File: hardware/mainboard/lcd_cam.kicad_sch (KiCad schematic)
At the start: 59 parts

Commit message: ERC fixes
Signed-off-by: gatecat <gatecat@ds0.me>
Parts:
- gave numbers to parts that had none: 59
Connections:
- net DSI0A_D0-: no longer LCD2.11 (DSI_D0-_A)
- net FRONT_LCD_TE renamed RIGHT_LCD_TE
- new net DSI1A_D0-: LCD2.11 (DSI_D0-_A)

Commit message: Add some footprint mappings
Signed-off-by: gatecat <gatecat@ds0.me>
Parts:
- C65, C66, C69, C70: footprint (none) -> Capacitor_SMD:C_0402_1005Metric
- C67, C74, C75: footprint (none) -> Capacitor_SMD:C_1206_3216Metric
- C68, C71, C72, C73, C76: footprint (none) -> Capacitor_SMD:C_0603_1608Metric
- CAM1, CAM2: footprint (none) -> meowality:54548-2271
- D20, D21, D22: footprint (none) -> Diode_SMD:D_SMA
- L6, L8: footprint (none) -> Inductor_SMD:L_Taiyo-Yuden_NR-50xx
- LCD1, LCD2: footprint (none) -> meowality:245863060104829
- R63, R64, R65, R66, R67, R68, R69, R70, R71, R72, R73, R74, R75, R76, R77, R78, R79, R80, R81, R82, R83, R84, R85, R86, R87, R88, R89, R90, R91, R92, R93, R94: footprint (none) -> Resistor_SMD:R_0402_1005Metric

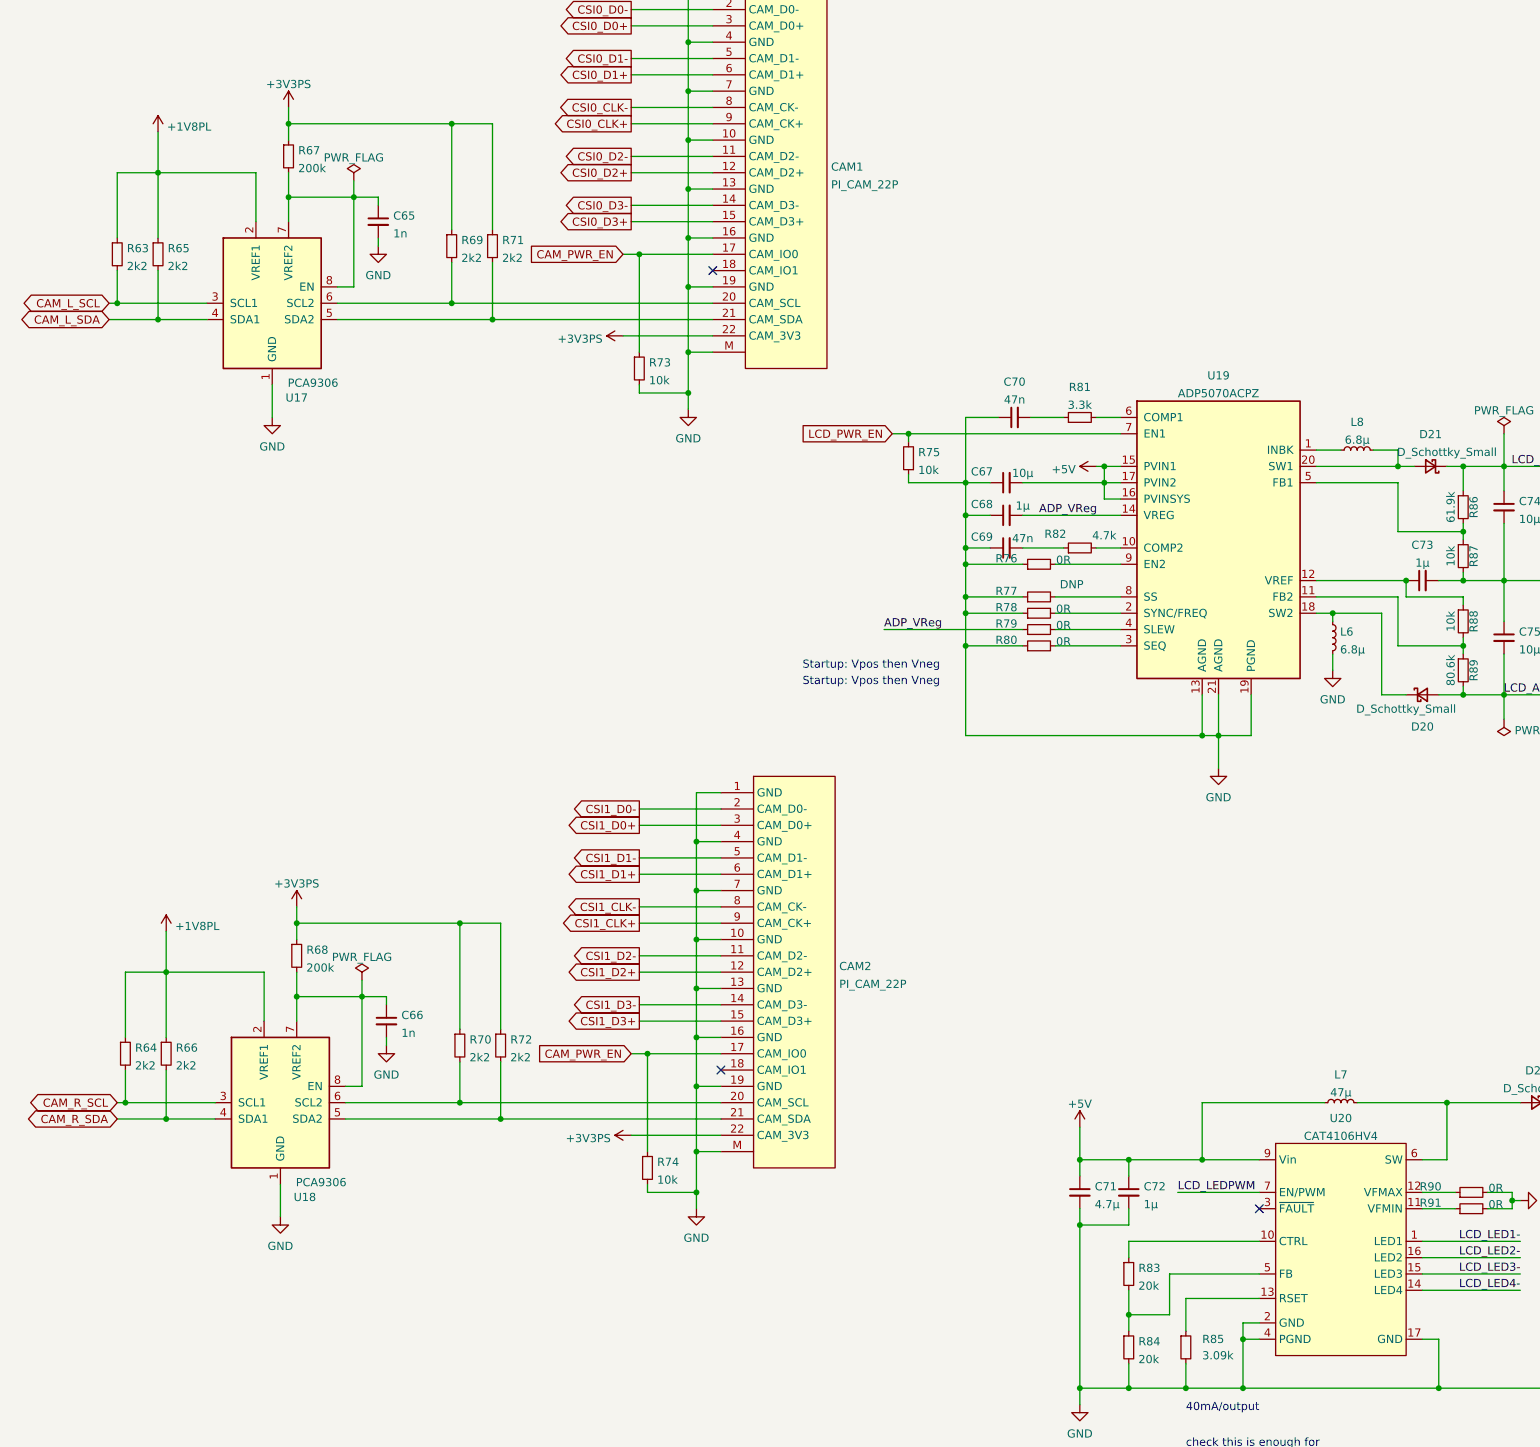
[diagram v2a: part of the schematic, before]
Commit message: Footprint assignments and related fixes
Signed-off-by: gatecat <gatecat@ds0.me>
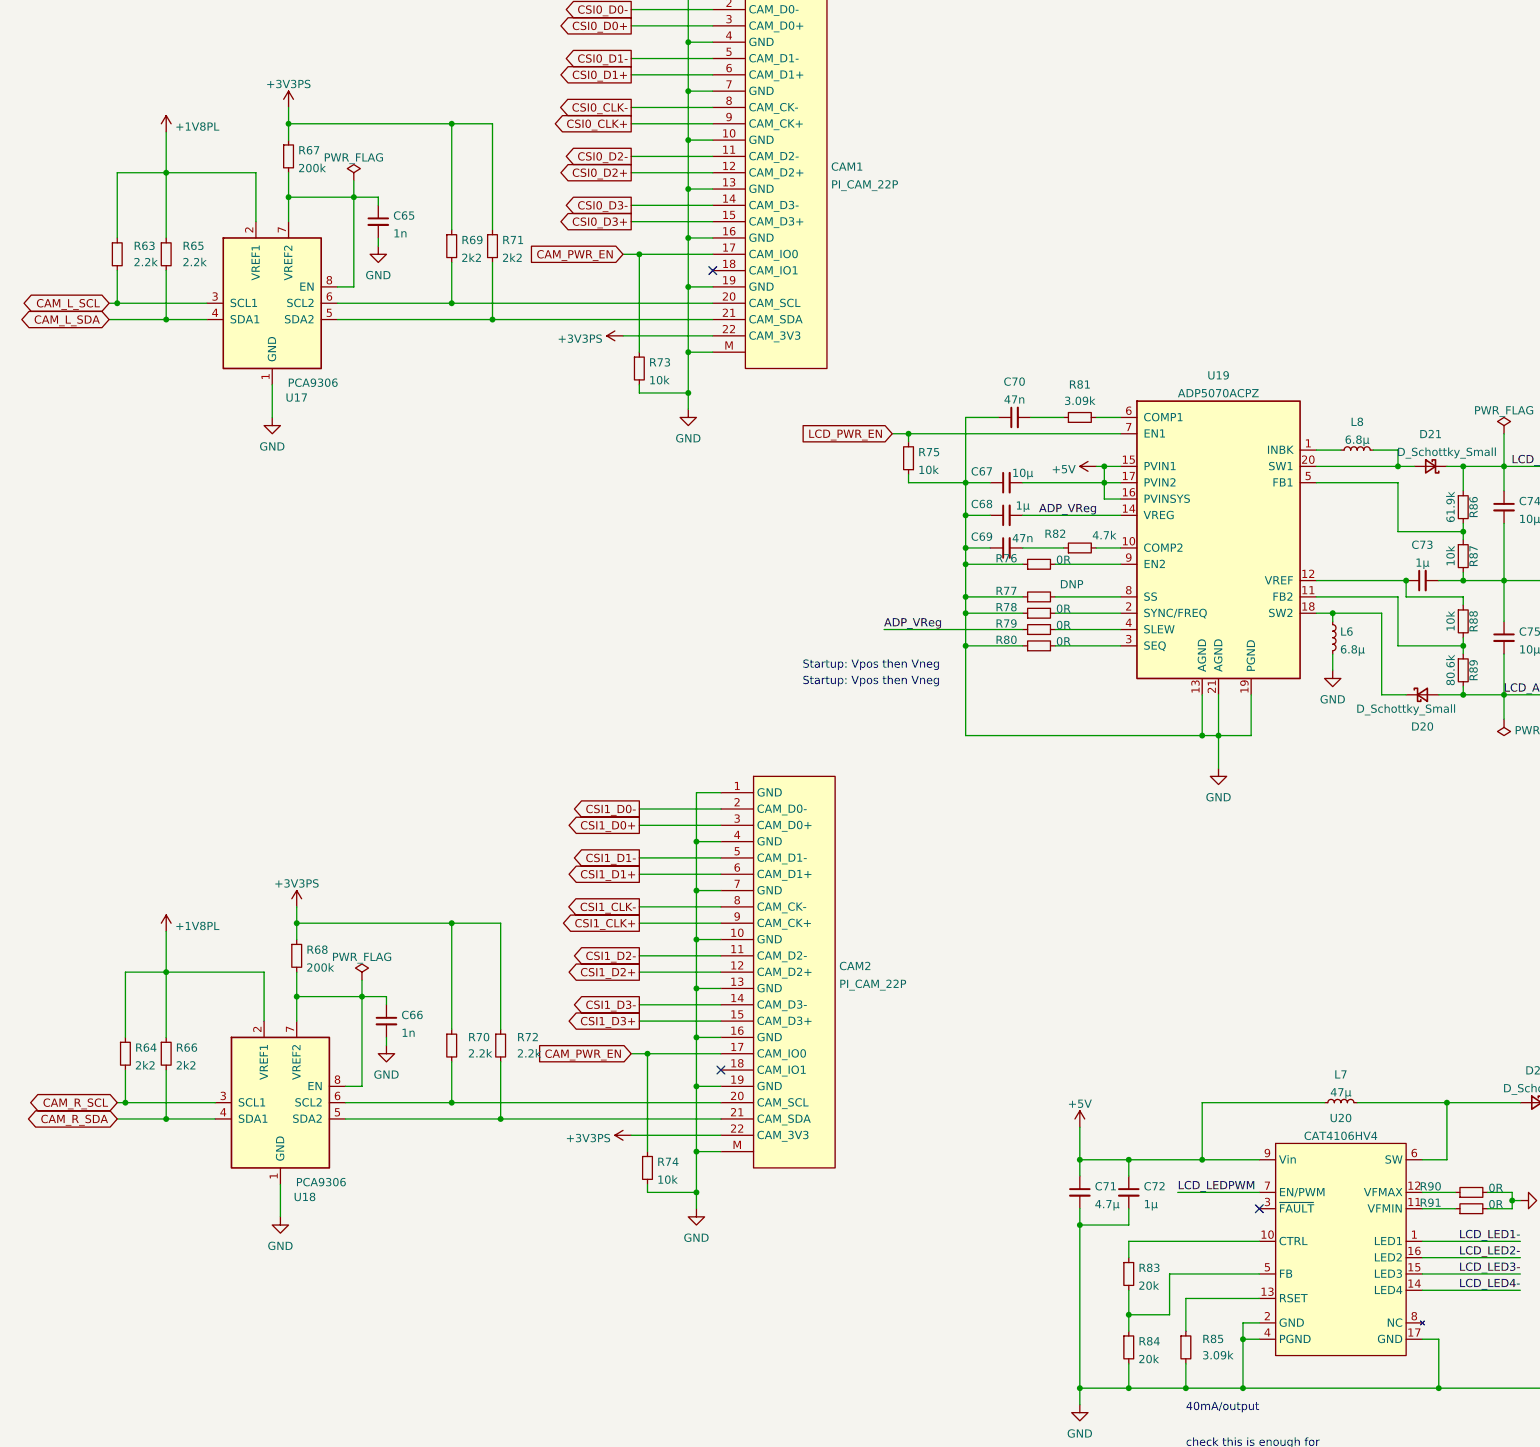
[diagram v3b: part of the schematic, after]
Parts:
- R63, R65, R70, R72: value 2k2 -> 2.2k
- R81: value 3.3k -> 3.09k
- TP1: footprint (none) -> TestPoint:TestPoint_Pad_D2.0mm
- U17, U18: footprint (none) -> Package_SO:TSSOP-8_3x3mm_P0.65mm
- U19: footprint (none) -> Package_DFN_QFN:QFN-20-1EP_4x4mm_P0.5mm_EP2.6x2.6mm
- U20: footprint (none) -> Package_DFN_QFN:QFN-16-1EP_4x4mm_P0.65mm_EP2.1x2.1mm
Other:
- moved on the sheet: R65, R70
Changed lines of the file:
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@@
   (junction (at 201.93 234.95) (diameter 0) (color 0 0 0 0)
   )
-  (junction (at 97.79 201.93) (diameter 0) (color 0 0 0 0)
+  (junction (at 96.52 201.93) (diameter 0) (color 0 0 0 0)
   )
   (junction (at 176.53 118.11) (diameter 0) (color 0 0 0 0)
@@
   (junction (at 72.39 185.42) (diameter 0) (color 0 0 0 0)
   )
-  (junction (at 97.79 173.99) (diameter 0) (color 0 0 0 0)
+  (junction (at 96.52 173.99) (diameter 0) (color 0 0 0 0)
   )
   (junction (at 201.93 246.38) (diameter 0) (color 0 0 0 0)
@@
   (junction (at 52.07 181.61) (diameter 0) (color 0 0 0 0)
   )
-  (junction (at 50.8 57.15) (diameter 0) (color 0 0 0 0)
+  (junction (at 52.07 57.15) (diameter 0) (color 0 0 0 0)
   )
   (junction (at 176.53 115.57) (diameter 0) (color 0 0 0 0)
@@
   (junction (at 356.87 31.75) (diameter 0) (color 0 0 0 0)
   )
-  (junction (at 50.8 80.01) (diameter 0) (color 0 0 0 0)
+  (junction (at 52.07 80.01) (diameter 0) (color 0 0 0 0)
   )
   (junction (at 254 138.43) (diameter 0) (color 0 0 0 0)
@@
     (stroke (width 0) (type default) (color 0 0 0 0))
   )
-  (wire (pts (xy 50.8 50.8) (xy 50.8 57.15))
+  (wire (pts (xy 52.07 50.8) (xy 52.07 57.15))
     (stroke (width 0) (type default) (color 0 0 0 0))
   )
@@
     (stroke (width 0) (type default) (color 0 0 0 0))
   )
-  (wire (pts (xy 50.8 57.15) (xy 66.04 57.15))
+  (wire (pts (xy 52.07 57.15) (xy 66.04 57.15))
     (stroke (width 0) (type default) (color 0 0 0 0))
   )
@@
     (stroke (width 0) (type default) (color 0 0 0 0))
   )
-  (wire (pts (xy 50.8 72.39) (xy 50.8 80.01))
+  (wire (pts (xy 52.07 72.39) (xy 52.07 80.01))
     (stroke (width 0) (type default) (color 0 0 0 0))
   )
@@
     (stroke (width 0) (type default) (color 0 0 0 0))
   )
-  (wire (pts (xy 44.45 57.15) (xy 50.8 57.15))
+  (wire (pts (xy 44.45 57.15) (xy 52.07 57.15))
     (stroke (width 0) (type default) (color 0 0 0 0))
   )
@@
     (stroke (width 0) (type default) (color 0 0 0 0))
   )
-  (wire (pts (xy 72.39 173.99) (xy 97.79 173.99))
+  (wire (pts (xy 72.39 173.99) (xy 96.52 173.99))
     (stroke (width 0) (type default) (color 0 0 0 0))
   )
@@
     (stroke (width 0) (type default) (color 0 0 0 0))
   )
-  (wire (pts (xy 97.79 195.58) (xy 97.79 201.93))
+  (wire (pts (xy 96.52 195.58) (xy 96.52 201.93))
     (stroke (width 0) (type default) (color 0 0 0 0))
   )
@@
     (stroke (width 0) (type default) (color 0 0 0 0))
   )
-  (wire (pts (xy 97.79 173.99) (xy 97.79 190.5))
+  (wire (pts (xy 96.52 173.99) (xy 96.52 190.5))
     (stroke (width 0) (type default) (color 0 0 0 0))
   )
@@
     (stroke (width 0) (type default) (color 0 0 0 0))
   )
-  (wire (pts (xy 97.79 201.93) (xy 138.43 201.93))
+  (wire (pts (xy 96.52 201.93) (xy 138.43 201.93))
     (stroke (width 0) (type default) (color 0 0 0 0))
   )
@@
     (stroke (width 0) (type default) (color 0 0 0 0))
   )
-  (wire (pts (xy 104.14 173.99) (xy 97.79 173.99))
+  (wire (pts (xy 104.14 173.99) (xy 96.52 173.99))
     (stroke (width 0) (type default) (color 0 0 0 0))
   )
@@
     (stroke (width 0) (type default) (color 0 0 0 0))
   )
-  (wire (pts (xy 43.18 80.01) (xy 50.8 80.01))
+  (wire (pts (xy 43.18 80.01) (xy 52.07 80.01))
     (stroke (width 0) (type default) (color 0 0 0 0))
   )
@@
     (stroke (width 0) (type default) (color 0 0 0 0))
   )
-  (wire (pts (xy 50.8 80.01) (xy 58.42 80.01))
+  (wire (pts (xy 52.07 80.01) (xy 58.42 80.01))
     (stroke (width 0) (type default) (color 0 0 0 0))
   )
@@
     (stroke (width 0) (type default) (color 0 0 0 0))
   )
-  (wire (pts (xy 80.01 201.93) (xy 97.79 201.93))
+  (wire (pts (xy 80.01 201.93) (xy 96.52 201.93))
     (stroke (width 0) (type default) (color 0 0 0 0))
   )
@@
     (stroke (width 0) (type default) (color 0 0 0 0))
   )
-  (wire (pts (xy 50.8 57.15) (xy 50.8 67.31))
+  (wire (pts (xy 52.07 57.15) (xy 52.07 67.31))
     (stroke (width 0) (type default) (color 0 0 0 0))
   )
@@
     (pin "2")
   )
-  (symbol (lib_id "meowality:+1V8PL") (at 50.8 50.8 0) (unit 1)
+  (symbol (lib_id "meowality:+1V8PL") (at 52.07 50.8 0) (unit 1)
     (in_bom yes) (on_board yes) (fields_autoplaced)
-    (property "Reference" "#PWR0354" (id 0) (at 50.8 54.61 0)
+    (property "Reference" "#PWR0354" (id 0) (at 52.07 54.61 0)
       (effects (font (size 1.27 1.27)) hide)
     )
-    (property "Value" "+1V8PL" (id 1) (at 52.197 50.009 0)
+    (property "Value" "+1V8PL" (id 1) (at 53.467 50.009 0)
       (effects (font (size 1.27 1.27)) (justify left))
     )
-    (property "Footprint" "" (id 2) (at 50.8 50.8 0)
+    (property "Footprint" "" (id 2) (at 52.07 50.8 0)
       (effects (font (size 1.27 1.27)) hide)
     )
-    (property "Datasheet" "" (id 3) (at 50.8 50.8 0)
+    (property "Datasheet" "" (id 3) (at 52.07 50.8 0)
       (effects (font (size 1.27 1.27)) hide)
     )
@@
       (effects (font (size 1.27 1.27)) (justify left))
     )
-    (property "Footprint" "" (id 2) (at 370.84 123.19 0)
+    (property "Footprint" "TestPoint:TestPoint_Pad_D2.0mm" (id 2) (at 370.84 123.19 0)
       (effects (font (size 1.27 1.27)) hide)
     )
@@
     (pin "M")
   )
-  (symbol (lib_id "Device:R_Small") (at 97.79 193.04 0) (unit 1)
+  (symbol (lib_id "Device:R_Small") (at 96.52 193.04 0) (unit 1)
     (in_bom yes) (on_board yes) (fields_autoplaced)
-    (property "Reference" "R70" (id 0) (at 99.2886 192.1315 0)
+    (property "Reference" "R70" (id 0) (at 99.06 191.7699 0)
       (effects (font (size 1.27 1.27)) (justify left))
     )
-    (property "Value" "2k2" (id 1) (at 99.2886 194.9066 0)
+    (property "Value" "2.2k" (id 1) (at 99.06 194.3099 0)
       (effects (font (size 1.27 1.27)) (justify left))
     )
-    (property "Footprint" "Resistor_SMD:R_0402_1005Metric" (id 2) (at 97.79 193.04 0)
+    (property "Footprint" "Resistor_SMD:R_0402_1005Metric" (id 2) (at 96.52 193.04 0)
       (effects (font (size 1.27 1.27)) hide)
     )
-    (property "Datasheet" "~" (id 3) (at 97.79 193.04 0)
+    (property "Datasheet" "~" (id 3) (at 96.52 193.04 0)
       (effects (font (size 1.27 1.27)) hide)
     )
@@
   (symbol (lib_id "Device:R_Small") (at 104.14 193.04 0) (unit 1)
     (in_bom yes) (on_board yes) (fields_autoplaced)
-    (property "Reference" "R72" (id 0) (at 105.6386 192.1315 0)
+    (property "Reference" "R72" (id 0) (at 106.68 191.7699 0)
       (effects (font (size 1.27 1.27)) (justify left))
     )
-    (property "Value" "2k2" (id 1) (at 105.6386 194.9066 0)
+    (property "Value" "2.2k" (id 1) (at 106.68 194.3099 0)
       (effects (font (size 1.27 1.27)) (justify left))
     )
@@
   (symbol (lib_id "Device:R_Small") (at 44.45 69.85 0) (unit 1)
     (in_bom yes) (on_board yes) (fields_autoplaced)
-    (property "Reference" "R63" (id 0) (at 45.9486 68.9415 0)
+    (property "Reference" "R63" (id 0) (at 46.99 68.5799 0)
       (effects (font (size 1.27 1.27)) (justify left))
     )
-    (property "Value" "2k2" (id 1) (at 45.9486 71.7166 0)
+    (property "Value" "2.2k" (id 1) (at 46.99 71.1199 0)
       (effects (font (size 1.27 1.27)) (justify left))
     )
@@
     (property "Reference" "U20" (id 0) (at 234.95 204.3643 0))
     (property "Value" "CAT4106HV4" (id 1) (at 234.95 207.1394 0))
-    (property "Footprint" "" (id 2) (at 234.95 241.3 0)
+    (property "Footprint" "Package_DFN_QFN:QFN-16-1EP_4x4mm_P0.65mm_EP2.1x2.1mm" (id 2) (at 234.95 241.3 0)
       (effects (font (size 1.27 1.27)) hide)
     )
@@
     (pin "6")
     (pin "7")
+    (pin "8")
     (pin "9")
   )
@@
     (pin "2")
   )
-  (symbol (lib_id "Device:R_Small") (at 50.8 69.85 0) (unit 1)
+  (symbol (lib_id "Device:R_Small") (at 52.07 69.85 0) (unit 1)
     (in_bom yes) (on_board yes) (fields_autoplaced)
-    (property "Reference" "R65" (id 0) (at 52.2986 68.9415 0)
+    (property "Reference" "R65" (id 0) (at 54.61 68.5799 0)
       (effects (font (size 1.27 1.27)) (justify left))
     )
-    (property "Value" "2k2" (id 1) (at 52.2986 71.7166 0)
+    (property "Value" "2.2k" (id 1) (at 54.61 71.1199 0)
       (effects (font (size 1.27 1.27)) (justify left))
     )
-    (property "Footprint" "Resistor_SMD:R_0402_1005Metric" (id 2) (at 50.8 69.85 0)
+    (property "Footprint" "Resistor_SMD:R_0402_1005Metric" (id 2) (at 52.07 69.85 0)
       (effects (font (size 1.27 1.27)) hide)
     )
-    (property "Datasheet" "~" (id 3) (at 50.8 69.85 0)
+    (property "Datasheet" "~" (id 3) (at 52.07 69.85 0)
       (effects (font (size 1.27 1.27)) hide)
     )
@@
     (property "Reference" "U17" (id 0) (at 72.39 92.1926 0))
     (property "Value" "PCA9306" (id 1) (at 74.93 89.8877 0))
-    (property "Footprint" "" (id 2) (at 58.42 68.58 0)
+    (property "Footprint" "Package_SO:TSSOP-8_3x3mm_P0.65mm" (id 2) (at 58.42 68.58 0)
       (effects (font (size 1.27 1.27)) hide)
     )
@@
     (property "Reference" "U18" (id 0) (at 73.66 216.6526 0))
     (property "Value" "PCA9306" (id 1) (at 76.2 214.3477 0))
-    (property "Footprint" "" (id 2) (at 59.69 193.04 0)
+    (property "Footprint" "Package_SO:TSSOP-8_3x3mm_P0.65mm" (id 2) (at 59.69 193.04 0)
       (effects (font (size 1.27 1.27)) hide)
     )
@@
   )
   (symbol (lib_id "Device:R_Small") (at 194.31 95.25 90) (unit 1)
-    (in_bom yes) (on_board yes) (fields_autoplaced)
-    (property "Reference" "R81" (id 0) (at 194.31 90.5469 90))
-    (property "Value" "3.3k" (id 1) (at 194.31 93.322 90))
+    (in_bom yes) (on_board yes)
+    (property "Reference" "R81" (id 0) (at 194.31 90.17 90))
+    (property "Value" "3.09k" (id 1) (at 194.31 92.71 90))
     (property "Footprint" "Resistor_SMD:R_0402_1005Metric" (id 2) (at 194.31 95.25 0)
       (effects (font (size 1.27 1.27)) hide)
@@
     (property "Reference" "U19" (id 0) (at 215.9 88.7434 0))
     (property "Value" "ADP5070ACPZ" (id 1) (at 215.9 91.5185 0))
-    (property "Footprint" "" (id 2) (at 217.17 140.97 0)
+    (property "Footprint" "Package_DFN_QFN:QFN-20-1EP_4x4mm_P0.5mm_EP2.6x2.6mm" (id 2) (at 217.17 140.97 0)
       (effects (font (size 1.27 1.27)) hide)
     )
